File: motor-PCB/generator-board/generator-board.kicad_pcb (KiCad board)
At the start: 2 copper layers, 142 x 70 mm, 31 parts, among them J1 Conn_02x05_Odd_Even, J2 Conn_01x02, Q1 PMOS, Q10 NMOS, Q6 NMOS, Q7 NMOS, Q8 NMOS, Q9 NMOS, U2 TMP117xxDRV, U3 INA219BxDCN

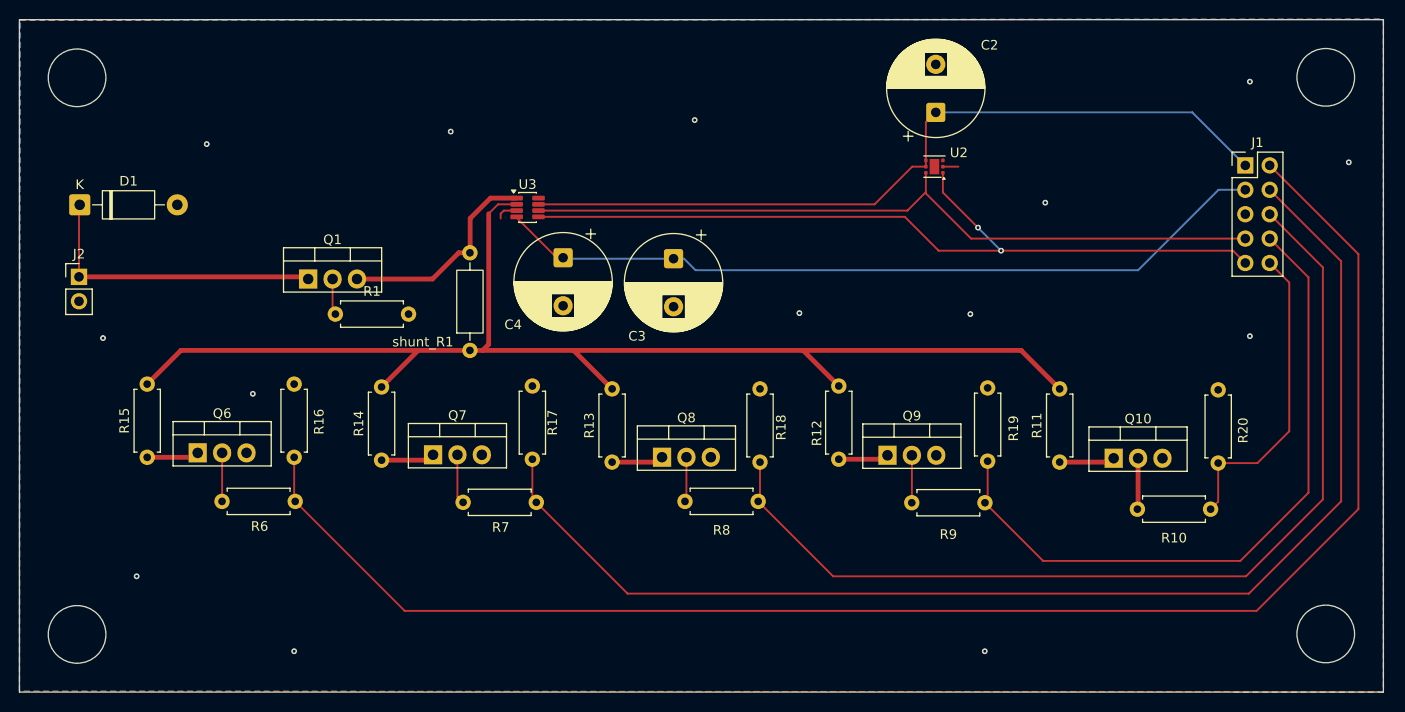
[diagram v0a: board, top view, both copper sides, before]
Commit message: added a missing capacitor in the control-board. Added pins to be able to control the heating pad and fan and text. In the generator changed the transistor layout and also added text
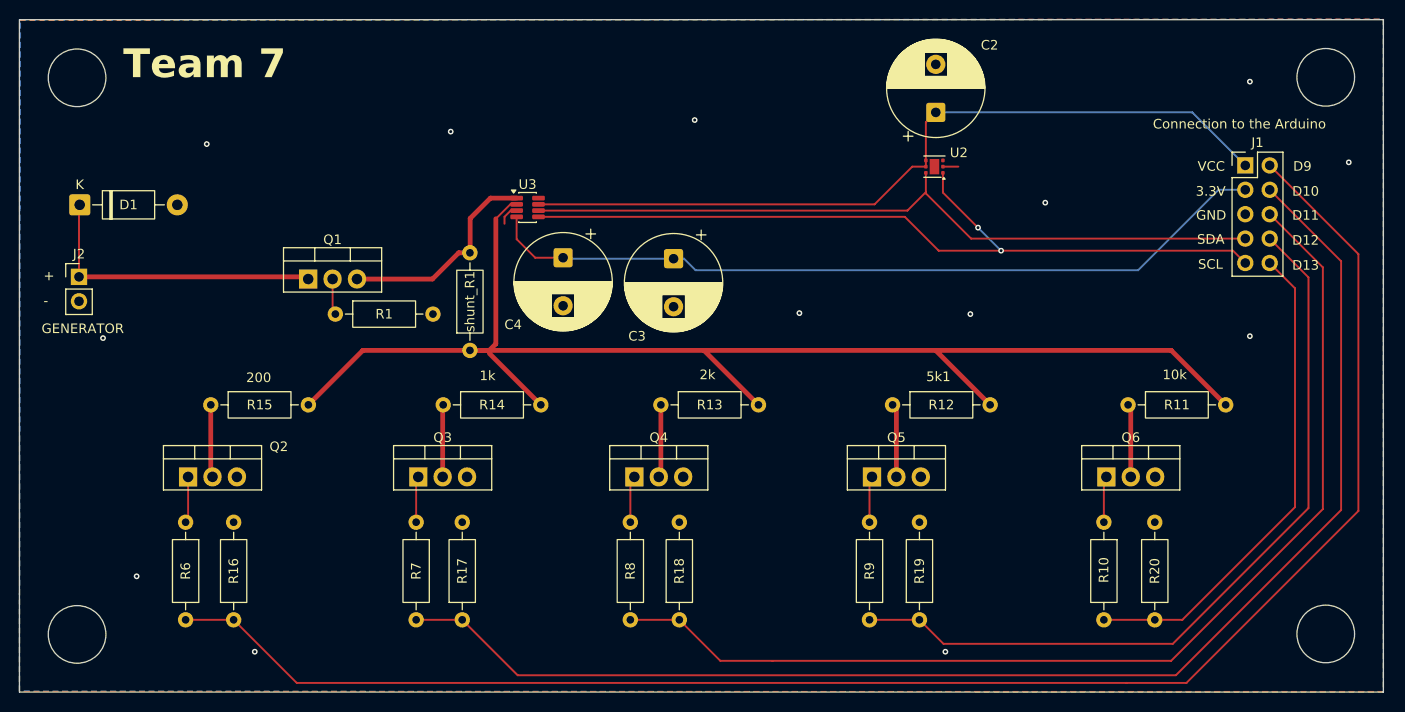
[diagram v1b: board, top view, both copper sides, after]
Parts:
- removed Q10, Q7, Q8, Q9: NMOS, Package_TO_SOT_THT:TO-220-3_Vertical
- added Q2: NMOS_GDS, Package_TO_SOT_THT:TO-220-3_Vertical, F.Cu at (116.0, 88.7)
- added Q3: NMOS_GDS, Package_TO_SOT_THT:TO-220-3_Vertical, F.Cu at (139.9, 88.7)
- added Q4: NMOS_GDS, Package_TO_SOT_THT:TO-220-3_Vertical, F.Cu at (162.4, 88.7)
- added Q5: NMOS_GDS, Package_TO_SOT_THT:TO-220-3_Vertical, F.Cu at (187.2, 88.7)
- Q6: value NMOS -> NMOS_GDS
- R1, R10, R11, R13, R14, R6, R7, R8, R9: footprint Resistor_THT:R_Axial_DIN0207_L6.3mm_D2.5mm_P7.62mm_Horizontal -> Resistor_THT:R_Axial_DIN0207_L6.3mm_D2.5mm_P10.16mm_Horizontal
- R12: value 5k -> 5k1; footprint Resistor_THT:R_Axial_DIN0207_L6.3mm_D2.5mm_P7.62mm_Horizontal -> Resistor_THT:R_Axial_DIN0207_L6.3mm_D2.5mm_P10.16mm_Horizontal
- R15: value 100 -> 200; footprint Resistor_THT:R_Axial_DIN0207_L6.3mm_D2.5mm_P7.62mm_Horizontal -> Resistor_THT:R_Axial_DIN0207_L6.3mm_D2.5mm_P10.16mm_Horizontal
- R16, R17, R18, R19, R20: value 40k -> 47k; footprint Resistor_THT:R_Axial_DIN0207_L6.3mm_D2.5mm_P7.62mm_Horizontal -> Resistor_THT:R_Axial_DIN0207_L6.3mm_D2.5mm_P10.16mm_Horizontal
- moved Q6 94.6 mm to (211.6, 88.7)
- moved R18 18.4 mm to (167.1, 103.5)
- moved R17 18.2 mm to (144.5, 103.5)
- moved R16 18.1 mm to (120.7, 103.5)
- moved R19 18.0 mm to (192.1, 103.5)
- moved R20 17.6 mm to (216.6, 103.5)
- moved R11 9.29 mm to (213.8, 81.2), turned to 0 degrees
- moved R14 8.63 mm to (142.5, 81.2), turned to 0 degrees
- moved R15 8.58 mm to (118.3, 81.2), turned to 0 degrees
- moved R12 7.96 mm to (189.3, 81.2), turned to 0 degrees
- moved R13 7.83 mm to (165.2, 81.2), turned to 0 degrees
- moved R8 6.09 mm to (162.0, 93.4), turned to -90 degrees
- moved R7 5.31 mm to (139.7, 93.4), turned to -90 degrees
- moved R9 4.85 mm to (186.9, 93.4), turned to -90 degrees
- moved R6 4.37 mm to (115.7, 93.4), turned to -90 degrees
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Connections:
- Q6 pad 1: Net-(Q6-D) -> Net-(Q6-G)
- Q6 pad 2: Net-(Q6-G) -> Net-(Q6-D)
- R10 pad 1: Net-(Q10-G) -> Net-(Q6-G)
- R11 pad 1: Net-(Q10-D) -> Net-(Q6-D)
- R15 pad 1: Net-(Q6-D) -> Net-(Q2-D)
- R6 pad 1: Net-(Q6-G) -> Net-(Q2-G)
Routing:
- net /D13: track 32.3 -> 51.3 mm
- net /D11: track 101.5 -> 113.4 mm
- net /D12: track 71.7 -> 82.3 mm
- net /D10: track 131.9 -> 142.2 mm
- net /IN-: track 133.5 -> 142.9 mm
- net /D9: track 164.0 -> 172.1 mm
- net Net-(Q2-D): track 0.00 -> 7.57 mm
- net Net-(Q10-D): track 5.79 -> 0.00 mm
- net Net-(Q10-G): track 5.33 -> 0.00 mm
- net Net-(Q2-G): track 0.00 -> 4.83 mm
- net Net-(Q5-D): track 5.24 -> 7.67 mm
- net Net-(Q4-D): track 5.41 -> 7.59 mm
- net Net-(Q6-D): track 5.45 -> 7.62 mm
- net Net-(Q3-D): track 5.59 -> 7.52 mm
- net +3.3V: track 81.7 -> 83.0 mm
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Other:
- board text added: "+"
- board text added: "-"
- board text added: "10k"
- board text added: "1k"
- board text added: "200"
- board text added: "2k"
- board text added: "3.3V"
- board text added: "5k1"
- board text added: "Connection to the Arduino"
- board text added: "D10"
- board text added: "D11"
- board text added: "D12"
- board text added: "D13"
- board text added: "D9"
- board text added: "GENERATOR"
- board text added: "GND"
- board text added: "SCL"
- board text added: "SDA"
- board text added: "Team 7"
- board text added: "VCC"

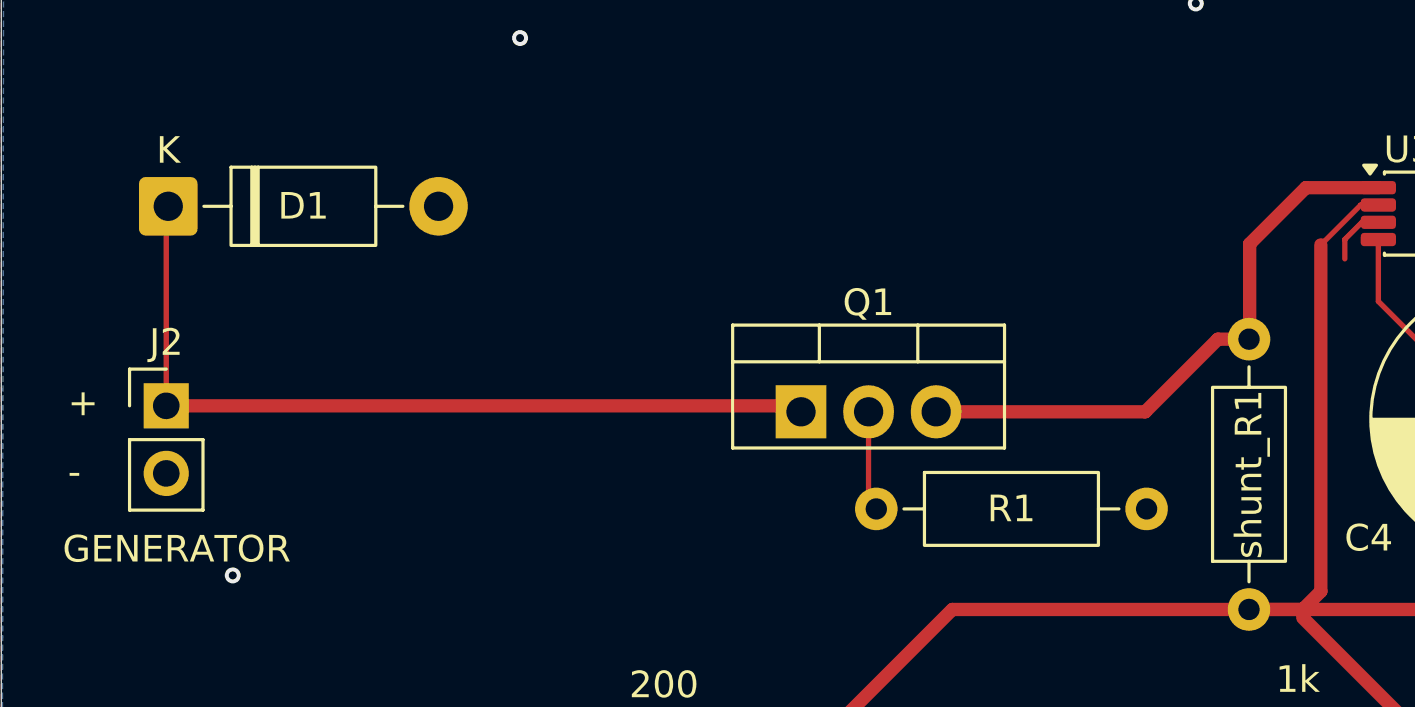
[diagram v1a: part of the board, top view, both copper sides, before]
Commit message: forgot to change the layout of the pmos so fixed that
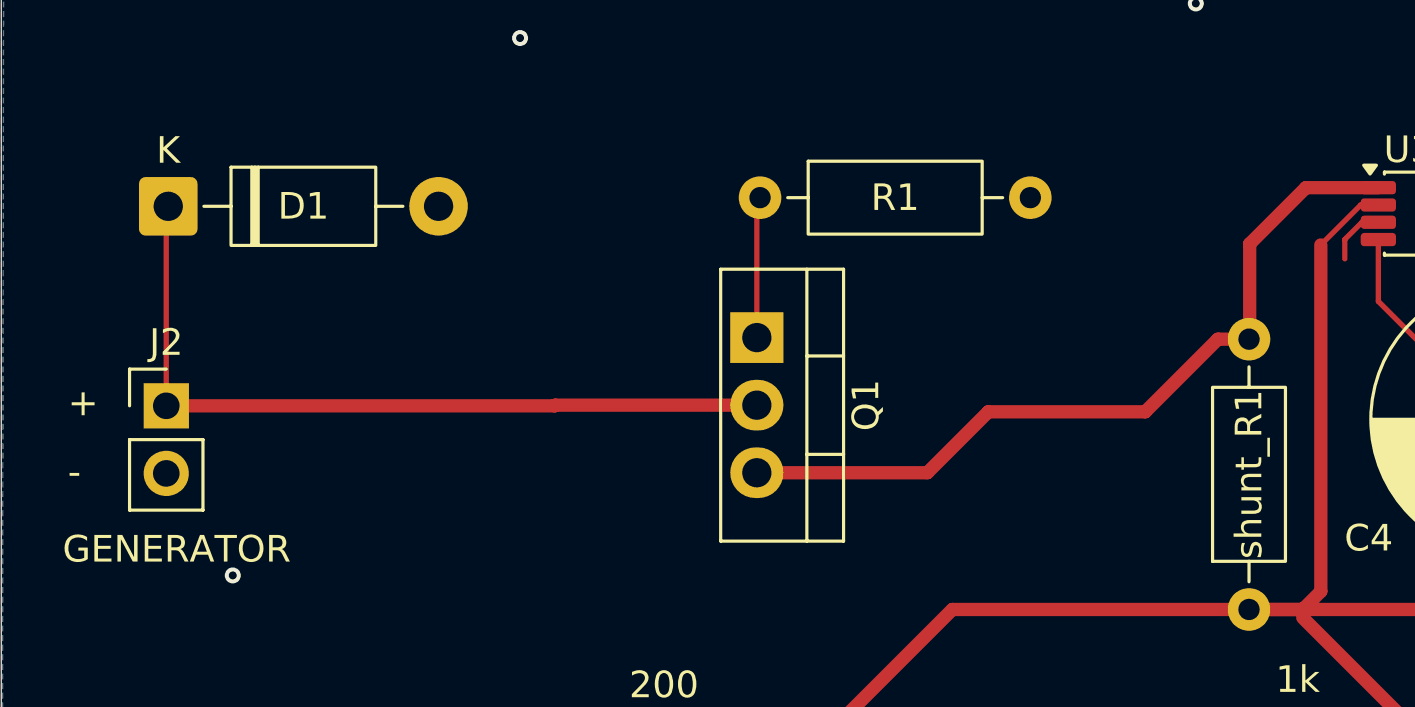
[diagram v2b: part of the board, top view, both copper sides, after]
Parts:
- moved R1 12.5 mm to (126.9, 60.0)
- moved Q1 3.25 mm to (126.8, 65.3), turned to -90 degrees
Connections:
- Q1 pad 1: /GENERATOR_IN -> Net-(Q1-G)
- Q1 pad 2: Net-(Q1-G) -> /GENERATOR_IN
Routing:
- net Net-(Q1-S): track 22.2 -> 29.9 mm
- net /GENERATOR_IN: track 31.5 -> 29.7 mm
- net Net-(Q1-G): track 3.77 -> 5.31 mm
